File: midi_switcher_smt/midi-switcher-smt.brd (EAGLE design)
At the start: 104.1 x 41.9 mm, 79 parts, among them IC1 6N138, IC2 PIC16F1825SO14, IC3 LD1086, Q1 MJD122GDPAK, Q2 MJD122GDPAK, Q3 MJD122GDPAK, Q4 MJD122GDPAK, Q5 MJD122GDPAK, Q6 MJD122GDPAK, Q7 MJD122GDPAK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

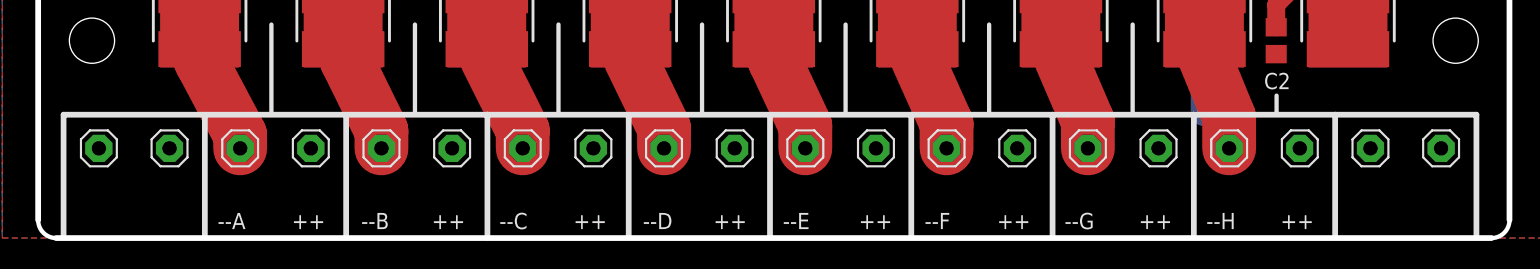
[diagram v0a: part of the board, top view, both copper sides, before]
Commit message: Rev 3B board (single) enlarge terminal pin holes
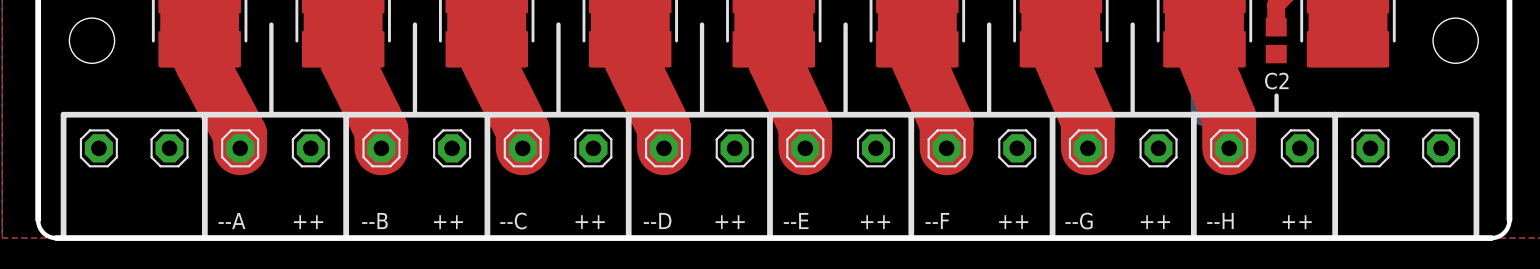
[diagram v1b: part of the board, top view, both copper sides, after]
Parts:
- OP1+, OP1-, OP2+, OP2-, OP3+, OP3-, OP4+, OP4-, OP5+, OP5-, OP6-, OP7+, OP7-, OP8+, OP8+1, OP8-, POWER+1, POWER+2, POWER-1, POWER-2: device adafruit:1X01 -> jason_eagle6:1X01W
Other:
- board text added: "PCB REV 3B"
- board text removed: "Mini Module REV3"
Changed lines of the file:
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@@
 <grid distance="1" unitdist="mil" unit="mil" style="lines" multiple="1" display="yes" altdistance="0.005" altunitdist="inch" altunit="inch"/>
 <layers>
-<layer number="1" name="Top" color="4" fill="1" visible="no" active="yes"/>
+<layer number="1" name="Top" color="4" fill="1" visible="yes" active="yes"/>
 <layer number="2" name="Route2" color="1" fill="3" visible="no" active="no"/>
 <layer number="3" name="Route3" color="4" fill="3" visible="no" active="no"/>
@@
 <layer number="56" name="wert" color="7" fill="1" visible="yes" active="yes"/>
 <layer number="57" name="tCAD" color="7" fill="1" visible="no" active="no"/>
+<layer number="90" name="Modules" color="7" fill="1" visible="yes" active="yes"/>
 <layer number="91" name="Nets" color="2" fill="1" visible="no" active="no"/>
 <layer number="92" name="Busses" color="1" fill="1" visible="no" active="no"/>
@@
 <text x="92.075" y="32.512" size="1.143" layer="25" font="vector" ratio="20" rot="R90">PWR SEL</text>
 <text x="84.582" y="27.051" size="1.143" layer="25" font="vector" ratio="20" rot="R180">MODE</text>
-<text x="105.791" y="13.843" size="1.778" layer="22" font="vector" ratio="20" rot="MR0">Mini Module REV3</text>
+<text x="105.791" y="13.843" size="1.778" layer="22" font="vector" ratio="20" rot="MR0">PCB REV 3B</text>
 <text x="105.664" y="11.176" size="1.778" layer="22" font="vector" ratio="20" rot="MR0">hotchk155</text>
 <text x="105.664" y="8.763" size="1.778" layer="22" font="vector" ratio="20" rot="MR0">six4pix.com/switcher</text>
@@
 <attribute name="VALUE" x="49.53" y="34.925" size="1.27" layer="27"/>
 </element>
-<element name="OP1-" library="adafruit" package="1X01" value="" x="97" y="5.08" smashed="yes">
+<element name="OP1-" library="jason_eagle6" package="1X01W" value="" x="97" y="5.08" smashed="yes">
 <attribute name="VALUE" x="95.73" y="1.905" size="1.27" layer="27"/>
 </element>
-<element name="OP2-" library="adafruit" package="1X01" value="" x="87" y="5.08" smashed="yes">
+<element name="OP2-" library="jason_eagle6" package="1X01W" value="" x="87" y="5.08" smashed="yes">
 <attribute name="VALUE" x="85.73" y="1.905" size="1.27" layer="27"/>
 </element>
-<element name="OP3-" library="adafruit" package="1X01" value="" x="77" y="5.08" smashed="yes">
+<element name="OP3-" library="jason_eagle6" package="1X01W" value="" x="77" y="5.08" smashed="yes">
 <attribute name="VALUE" x="75.73" y="1.905" size="1.27" layer="27"/>
 </element>
-<element name="OP4-" library="adafruit" package="1X01" value="" x="67" y="5.08" smashed="yes">
+<element name="OP4-" library="jason_eagle6" package="1X01W" value="" x="67" y="5.08" smashed="yes">
 <attribute name="VALUE" x="65.73" y="1.905" size="1.27" layer="27"/>
 </element>
-<element name="OP5-" library="adafruit" package="1X01" value="" x="57" y="5.08" smashed="yes">
+<element name="OP5-" library="jason_eagle6" package="1X01W" value="" x="57" y="5.08" smashed="yes">
 <attribute name="VALUE" x="55.73" y="1.905" size="1.27" layer="27"/>
 </element>
-<element name="OP6-" library="adafruit" package="1X01" value="" x="47" y="5.08" smashed="yes">
+<element name="OP6-" library="jason_eagle6" package="1X01W" value="" x="47" y="5.08" smashed="yes">
 <attribute name="VALUE" x="45.73" y="1.905" size="1.27" layer="27"/>
 </element>
-<element name="OP7-" library="adafruit" package="1X01" value="" x="37" y="5.08" smashed="yes">
+<element name="OP7-" library="jason_eagle6" package="1X01W" value="" x="37" y="5.08" smashed="yes">
 <attribute name="VALUE" x="35.73" y="1.905" size="1.27" layer="27"/>
 </element>
-<element name="OP8-" library="adafruit" package="1X01" value="" x="27" y="5.08" smashed="yes">
+<element name="OP8-" library="jason_eagle6" package="1X01W" value="" x="27" y="5.08" smashed="yes">
 <attribute name="VALUE" x="25.73" y="1.905" size="1.27" layer="27"/>
 </element>
-<element name="OP1+" library="adafruit" package="1X01" value="" x="32" y="5.08" smashed="yes">
+<element name="OP1+" library="jason_eagle6" package="1X01W" value="" x="32" y="5.08" smashed="yes">
 <attribute name="VALUE" x="30.73" y="1.905" size="1.27" layer="27"/>
 </element>
-<element name="OP2+" library="adafruit" package="1X01" value="" x="102" y="5.08" smashed="yes">
+<element name="OP2+" library="jason_eagle6" package="1X01W" value="" x="102" y="5.08" smashed="yes">
 <attribute name="VALUE" x="100.73" y="1.905" size="1.27" layer="27"/>
 </element>
-<element name="OP3+" library="adafruit" package="1X01" value="" x="92" y="5.08" smashed="yes">
+<element name="OP3+" library="jason_eagle6" package="1X01W" value="" x="92" y="5.08" smashed="yes">
 <attribute name="VALUE" x="90.73" y="1.905" size="1.27" layer="27"/>
 </element>
-<element name="OP4+" library="adafruit" package="1X01" value="" x="82" y="5.08" smashed="yes">
+<element name="OP4+" library="jason_eagle6" package="1X01W" value="" x="82" y="5.08" smashed="yes">
 <attribute name="VALUE" x="80.73" y="1.905" size="1.27" layer="27"/>
 </element>
-<element name="OP5+" library="adafruit" package="1X01" value="" x="72" y="5.08" smashed="yes">
+<element name="OP5+" library="jason_eagle6" package="1X01W" value="" x="72" y="5.08" smashed="yes">
 <attribute name="VALUE" x="70.73" y="1.905" size="1.27" layer="27"/>
 </element>
-<element name="OP7+" library="adafruit" package="1X01" value="" x="52" y="5.08" smashed="yes">
+<element name="OP7+" library="jason_eagle6" package="1X01W" value="" x="52" y="5.08" smashed="yes">
 <attribute name="VALUE" x="50.73" y="1.905" size="1.27" layer="27"/>
 </element>
-<element name="OP8+" library="adafruit" package="1X01" value="" x="42" y="5.08" smashed="yes">
+<element name="OP8+" library="jason_eagle6" package="1X01W" value="" x="42" y="5.08" smashed="yes">
 <attribute name="VALUE" x="40.73" y="1.905" size="1.27" layer="27"/>
 </element>
@@
 <attribute name="NAME" x="105.029" y="35.814" size="1.143" layer="25" font="vector" ratio="20" rot="R180"/>
 </element>
-<element name="POWER+1" library="adafruit" package="1X01" value="" x="22" y="5.08" smashed="yes">
+<element name="POWER+1" library="jason_eagle6" package="1X01W" value="" x="22" y="5.08" smashed="yes">
 <attribute name="VALUE" x="20.73" y="1.905" size="1.27" layer="27"/>
 </element>
-<element name="POWER+2" library="adafruit" package="1X01" value="" x="17" y="5.08" smashed="yes">
+<element name="POWER+2" library="jason_eagle6" package="1X01W" value="" x="17" y="5.08" smashed="yes">
 <attribute name="VALUE" x="15.73" y="1.905" size="1.27" layer="27"/>
 </element>
-<element name="POWER-1" library="adafruit" package="1X01" value="" x="112" y="5.08" smashed="yes">
+<element name="POWER-1" library="jason_eagle6" package="1X01W" value="" x="112" y="5.08" smashed="yes">
 <attribute name="VALUE" x="110.73" y="1.905" size="1.27" layer="27"/>
 </element>
-<element name="POWER-2" library="adafruit" package="1X01" value="" x="107" y="5.08" smashed="yes">
+<element name="POWER-2" library="jason_eagle6" package="1X01W" value="" x="107" y="5.08" smashed="yes">
 <attribute name="VALUE" x="105.73" y="1.905" size="1.27" layer="27"/>
 </element>
@@
 <attribute name="VALUE" x="90.805" y="39.751" size="1.27" layer="27" rot="R270"/>
 </element>
-<element name="OP8+1" library="adafruit" package="1X01" value="" x="62" y="5.08" smashed="yes">
+<element name="OP8+1" library="jason_eagle6" package="1X01W" value="" x="62" y="5.08" smashed="yes">
 <attribute name="VALUE" x="60.73" y="1.905" size="1.27" layer="27"/>
 </element>
